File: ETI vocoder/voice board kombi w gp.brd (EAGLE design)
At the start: 160 x 59.8 mm, 170 parts, among them IC1 TL072P, IC1. TL072P, IC2 TL072P, IC2. TL072P, IC3 TL081P, IC3. TL081P, IC4 TL081P, IC4. TL081P, IC5 TL072P, IC6 LM13600AN, IC7 TL072P, IC7. TL072P, P1. C-OR-R050_075-030X100, P10. C-OR-R050_075-030X100, P13. C-OR-R050_075-030X100, P14. C-OR-R050_075-030X100, P16 C-OR-R050_075-030X100, P2. C-OR-R050_075-030X100, P5. C-OR-R050_075-030X100, P6. C-OR-R050_075-030X100, P8 C-OR-R050_075-030X100, P9. C-OR-R050_075-030X100, Q1 BF244C, Q1. BF244C, Q2 BC212L, Q2. BC212L

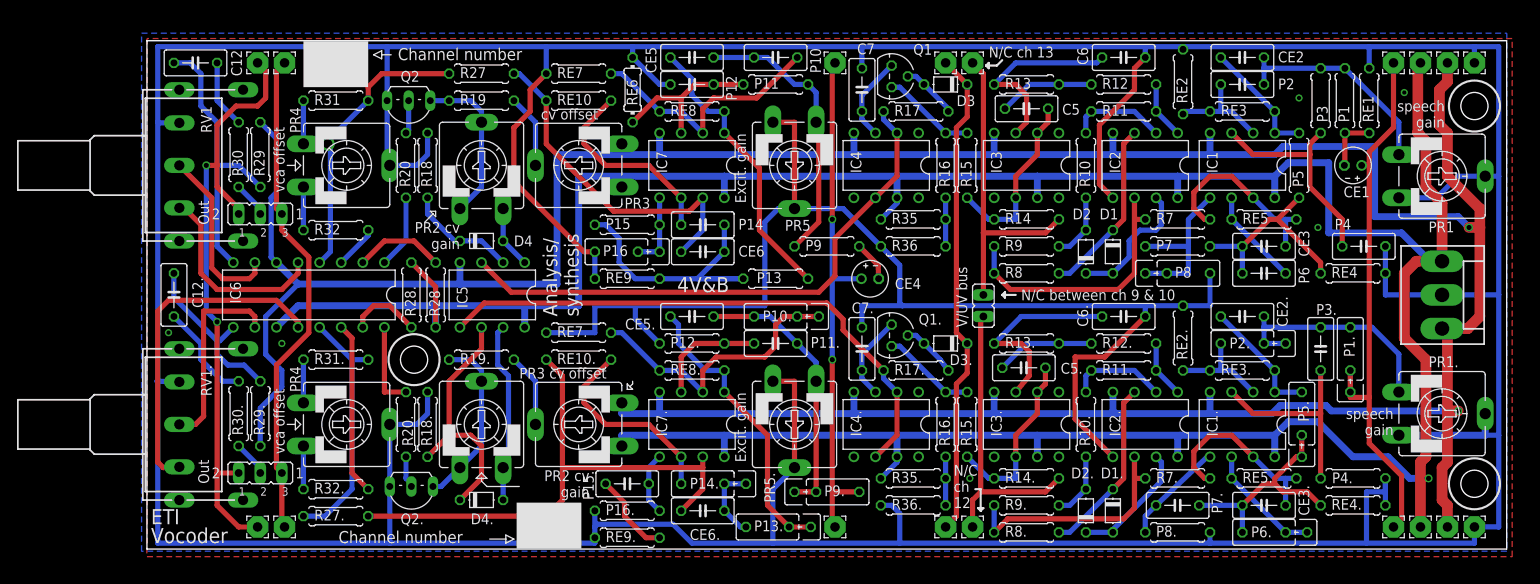
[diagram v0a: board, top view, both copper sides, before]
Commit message: Added four-legged transistor footprint to allow various JFETs. Changed all caps to 3.5mm wide
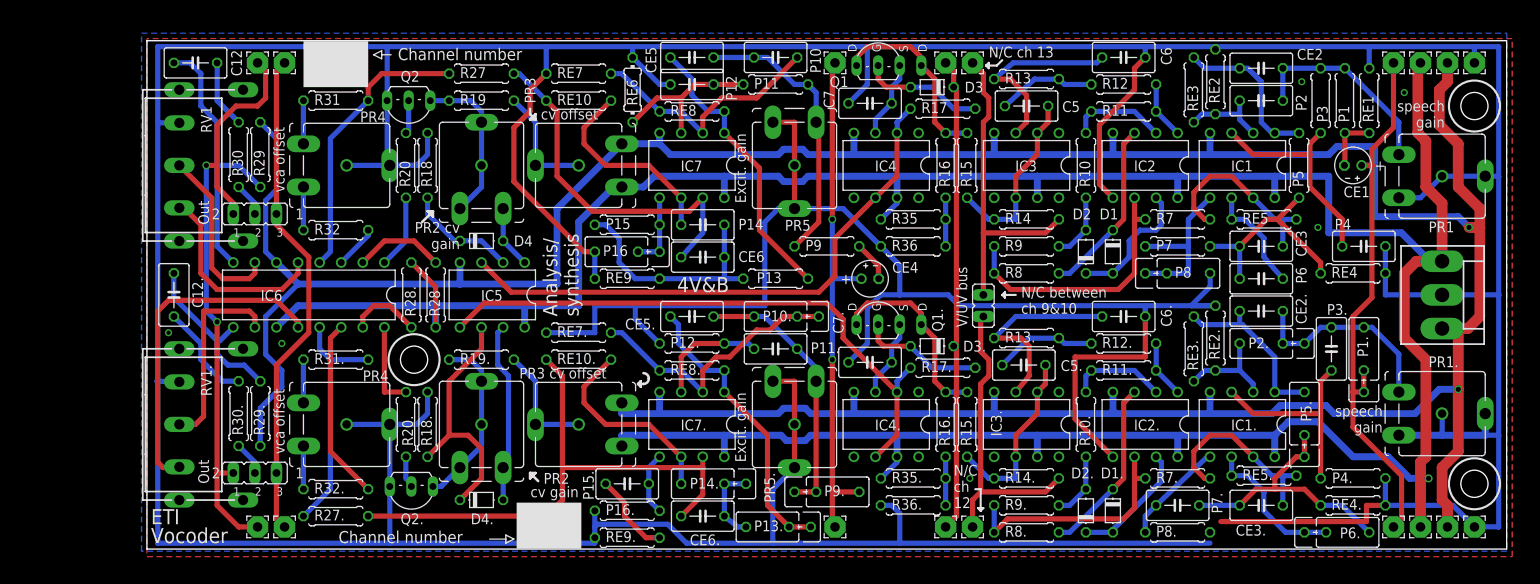
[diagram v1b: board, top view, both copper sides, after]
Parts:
- C12, C12., C5, C5., C6, C6., C7, C7., CE2, CE2., CE3, CE3., CE5, CE5., CE6, CE6., P10, P11., P12, P14, P15., P2, P3., P4, P6, P7.: device resistor:C050-030X075 -> resistor:C050-035X075
- P1., P10., P13., P14., P16, P2., P5., P6., P8, P9.: value C-OR-R050_075-030X100 -> C-OR-R050_075-035X100; device joakim:P050_075-030X100J -> joakim:P050_075-035X100J
- PR1, PR1., PR2, PR2., PR3, PR3., PR4, PR4., PR5, PR5.: device pot:CA9V -> joakim:MULTIPOT_2_J
- Q1, Q1.: device transistor-fet:TO-92 -> joakim:TO92-DGSD-J
- RV1, RV1.: device joakim:POT16_W_BRACKET -> joakim:POT16_W_BRACKET-J
- moved P6. 7.30 mm to (140.0, 2.22), turned to 180 degrees
- moved RE3 6.25 mm to (123.2, 54.3), turned to 90 degrees
- moved RE3. 6.25 mm to (123.2, 23.8), turned to 90 degrees
- moved RE2 3.81 mm to (125.7, 55.2)
- moved RE2. 3.81 mm to (125.7, 25.1)
- moved R17 3.19 mm to (93.7, 52.1)
- moved R17. 3.19 mm to (93.7, 21.6)
- moved P2 2.93 mm to (131.1, 53.0)
- moved CE2 2.56 mm to (131.1, 56.8)
- moved CE2. 2.31 mm to (131.1, 28.3)
- moved P2. 2.22 mm to (132.4, 24.4)
- moved Q1. 2.03 mm to (86.0, 26.7), turned to 0 degrees
- moved Q1 2.03 mm to (86.0, 57.1), turned to 0 degrees
- moved C7 1.85 mm to (85.1, 52.7), turned to 180 degrees
- moved C7. 1.85 mm to (85.1, 22.2), turned to 180 degrees
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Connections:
- net GND: now also PR1..S0, PR1.S0, PR4..S0, PR4.S0, PR5..S0, PR5.S0
- net N$17: now also Q1.D, Q1.D2; no longer Q1.3
- net N$18: now also Q1.S; no longer Q1.1
- net N$19: now also Q1.G; no longer Q1.2
- net N$23: now also PR2.S0
- net N$24: now also PR3.S0
- net N$63: now also Q1..D, Q1..D2; no longer Q1..3
- net N$64: now also Q1..S; no longer Q1..1
- net N$65: now also Q1..G; no longer Q1..2
- net N$69: now also PR2..S0
- net N$70: now also PR3..S0
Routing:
- net GND: track 798.5 -> 819.5 mm
- net N$63: track 11.1 -> 22.9 mm
- net N$17: track 11.1 -> 22.2 mm
- net N$65: track 6.58 -> 14.7 mm
- net N$19: track 6.66 -> 14.5 mm
- net N$28: track 34.8 -> 28.1 mm
- net N$49: track 14.7 -> 20.7 mm
- net +12V: track 374.4 -> 368.8 mm
- net N$70: track 8.67 -> 13.8 mm
- net N$24: track 8.67 -> 13.8 mm
- net N$3: track 14.4 -> 18.9 mm
- net N$50: track 27.0 -> 31.3 mm
- net N$66: track 66.9 -> 70.4 mm
- net N$48: track 27.4 -> 24.0 mm
- net N$51: track 14.1 -> 17.4 mm
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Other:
- board text added: "+"
- board text added: "D"
- board text added: "G"
- board text added: "N/C between ch 9&10"
- board text added: "PR2"
- board text added: "S"
- board text added: "cv gain"
- board text removed: "N/C between ch 9 & 10"

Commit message: Added optional decoupling capacitors. Still need to route and readd groundplanes
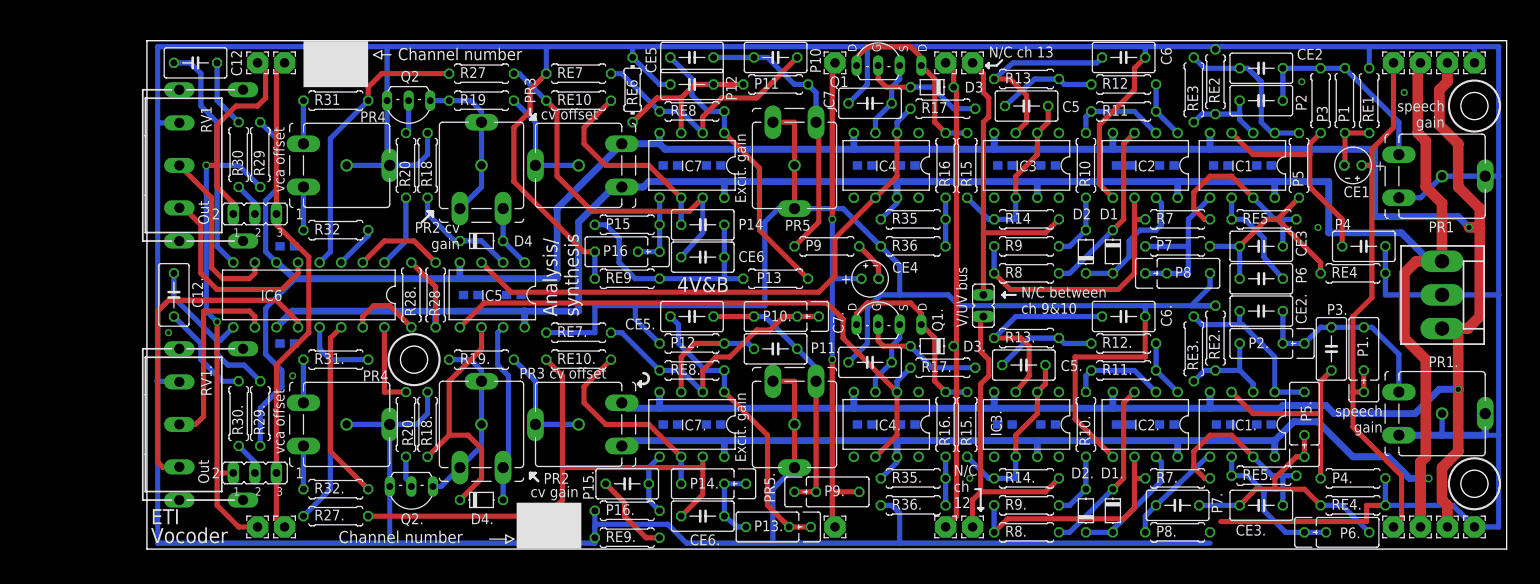
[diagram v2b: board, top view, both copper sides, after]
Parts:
- added C1, C10, C11, C13, C14, C15, C16, C17, C18, C19, C2, C20, C21, C22, C23, C24, C25, C26, C27, C28, C3, C4, C8, C9: 100nF, resistor:C0603
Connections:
- net +12V: now also C1.1, C10.1, C11.1, C13.1, C14.1, C15.1, C16.1, C2.1, C3.1, C4.1, C8.1, C9.1
- net -12V: now also C17.2, C18.2, C19.2, C20.2, C21.2, C22.2, C23.2, C24.2, C25.2, C26.2, C27.2, C28.2
- net GND: now also C1.2, C10.2, C11.2, C13.2, C14.2, C15.2, C16.2, C17.1, C18.1, C19.1, C2.2, C20.1, C21.1, C22.1, C23.1, C24.1, C25.1, C26.1, C27.1, C28.1, C3.2, C4.2, C8.2, C9.2
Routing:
- net -12V: track 398.5 -> 388.2 mm
- net +12V: track 368.8 -> 358.7 mm
- removed copper zone on layer 1, net GND
- removed copper zone on layer 16, net GND

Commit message: Routed and DRC/ERC'ed bypass caps
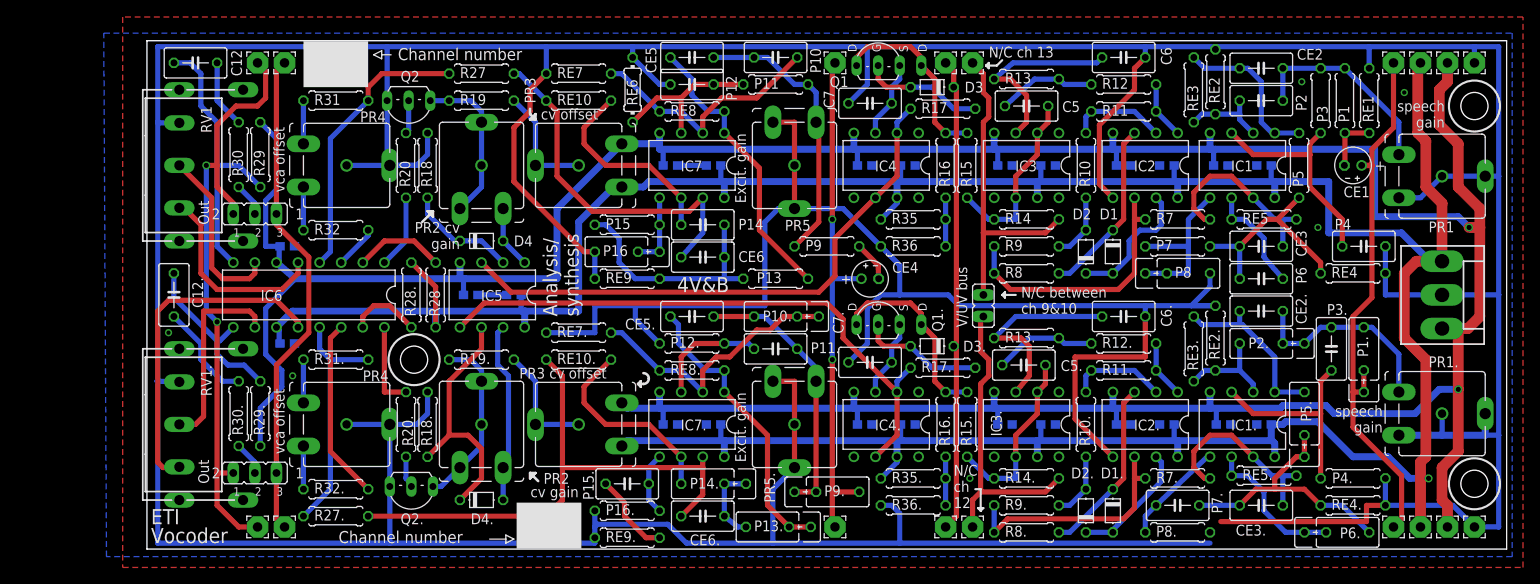
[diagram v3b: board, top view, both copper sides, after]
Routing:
- net -12V: track 388.2 -> 411.7 mm
- net +12V: track 358.7 -> 381.8 mm
- net GND: track 819.5 -> 826.2 mm
- added copper zone on layer 1, net GND
- added copper zone on layer 16, net GND

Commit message: Small cosmetic fixes
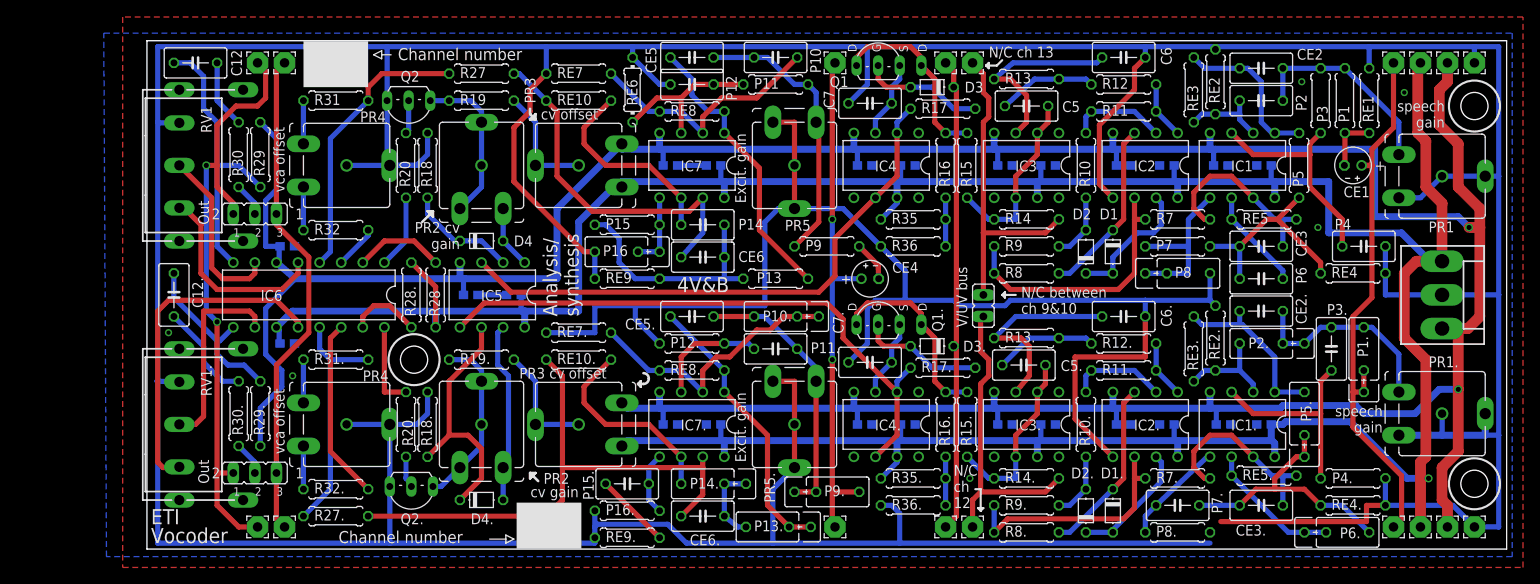
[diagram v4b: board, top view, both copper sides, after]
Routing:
- net GND: track 826.2 -> 823.3 mm
- net N$76: track 34.4 -> 33.1 mm
- net N$51: track 17.4 -> 16.1 mm
- net N$88: track 9.91 -> 8.98 mm
- net N$6: track 12.9 -> 12.0 mm
- net -12V: track 411.7 -> 412.3 mm
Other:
- board text added: "Analysis/synthesis board v1.0"
- board text added: "gnd"
- board text removed: "Dual voice board v1.0"
